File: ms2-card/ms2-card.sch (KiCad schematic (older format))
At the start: 41 parts, among them J1 Schaltregler, J10 MicroSD_SPI_CD, J11 I2C, J2 ESP Prog, J20 Smartcard Connector, J21 Card Edge, J22 Card Edge, J23 Conn_01x04, J3 RTS, J30 USB_B_Micro, J31 Power Select, J32 FTDI Adapter, J40 SP1, J50 Conn_01x05, J51 SP1, Q30 BC847, SW1 RESET, U1 ESP-12F, U30 CH330N, U40 ADUM1250, U41 ADuM1201AR

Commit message: wip
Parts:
- removed C1: 100uF, Capacitor_Tantalum_SMD:CP_EIA-7343-31_Kemet-D_Pad2.25x2.55mm_HandSolder, symbol Device:CP
- removed C30, C31, C40, C41, C50, C51: 100nF, Capacitors_SMD:C_0805_HandSoldering, symbol Device:C
- removed J1: Schaltregler, Connector_PinHeader_2.54mm:PinHeader_1x04_P2.54mm_Vertical, symbol Connector_Generic:Conn_01x04
- removed J2: ESP Prog, Connector_PinHeader_2.54mm:PinHeader_1x02_P2.54mm_Vertical, symbol Connector_Generic:Conn_01x02
- removed J3: RTS, Connector_PinHeader_2.54mm:PinHeader_1x01_P2.54mm_Vertical, symbol Connector_Generic:Conn_01x01
- removed J31: Power Select, Connector_PinHeader_2.54mm:PinHeader_1x03_P2.54mm_Vertical, symbol Connector_Generic:Conn_01x03
- removed J32: FTDI Adapter, Connector_PinSocket_2.54mm:PinSocket_1x06_P2.54mm_Horizontal, symbol Connector_Generic:Conn_01x06
- removed J40, J51: SP1, Connector_PinHeader_2.54mm:PinHeader_1x01_P2.54mm_Vertical, symbol Connector_Generic:Conn_01x01
- removed J50: Conn_01x05, Connector_PinHeader_2.54mm:PinHeader_1x05_P2.54mm_Vertical, symbol Connector_Generic:Conn_01x05
- removed R2, R50, R51: 4k7, Resistors_SMD:R_0805_HandSolderingII, symbol Device:R
- removed U1: ESP-12F, ESP8266:ESP-12E, symbol ESP8266:ESP-12F
- removed U30: CH330N, Package_SO:SOIC-8_3.9x4.9mm_P1.27mm, symbol Interface_USB:CH330N
- removed U40: ADUM1250, Package_SO:SOIC-8_3.9x4.9mm_P1.27mm, symbol Isolator:ADuM1201AR
- removed U41: ADuM1201AR, Package_SO:SOIC-8_3.9x4.9mm_P1.27mm, symbol Isolator:ADuM1201AR
- added Brd1: SSD1306, Lokkarten:128x64OLED, symbol Lokkarten:SSD1306
- added J1: Micro_SD_Card, w_conn_misc:GCT-MEM2055-00-190-01-A, symbol Connector:Micro_SD_Card
- added M1: PI_PICO_ZERO, Lokkarten:PI_PICO_ZERO, symbol Lokkarten:PI_PICO_ZERO
- added U1: W25Q128JVS, Package_SO:SOIC-8_5.23x5.23mm_P1.27mm, symbol Memory_Flash:W25Q128JVS
- J30: value USB_B_Micro -> Power Only
- SW1: value RESET -> SW_Push
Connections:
- net labels added: CS0, CS1
- net labels removed: CS, Card', GND2, GPIO0, LED, RxD, SCL', SDA', TxD, V3, VBUS, VDDA
- wire segments 180 -> 73
- no-connect marks 14 -> 5
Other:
- note removed: "Alternative zum CH330N"
- note removed: "Galvanische Trennung\nfür alt. RPi Interface"
- moved on the sheet: J21, J22, J30, Q30, R20, R21, R22, R23, R24

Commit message: new version with Pi Pico Zero
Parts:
- removed J1: Micro_SD_Card, w_conn_misc:GCT-MEM2055-00-190-01-A, symbol Connector:Micro_SD_Card
- removed J30: Power Only, Connector_USB:USB_Micro-B_Molex-105017-0001, symbol Connector:USB_B_Micro
- added C1: 100nF, Capacitor_SMD:C_0805_2012Metric_Pad1.18x1.45mm_HandSolder, symbol Device:C
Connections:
- net labels added: CLK0, CLK1, GP12, MISO0, MISO1, MOSI0, MOSI1, SCL0, SCL1, SDA0, SDA1
- net labels removed: CLK, MISO, MOSI, MS2PWR
- wire segments 73 -> 103
- no-connect marks 5 -> 14
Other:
- moved on the sheet: Brd1

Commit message: fix schematic
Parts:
- added C2: 100nF, Capacitor_SMD:C_0805_2012Metric_Pad1.18x1.45mm_HandSolder, symbol Device:C
- added J30: Power_Only, Connector_USB:USB_Micro-B_Molex-105017-0001, symbol Connector:USB_B_Micro
- added R2, R3: 4k7, Resistors_SMD:R_0805_HandSolderingII, symbol Device:R
- added R7, R8, R9: 47, Resistors_SMD:R_0805_HandSolderingII, symbol Device:R
- R6: renamed from R12; value 4k7 -> 47
- renumbered R11 to R4, R13 to R5
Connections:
- net SCL is gone; now on net SCL0: J20.3 (Pin_3)
- net SDA is gone; now on net SDA0: J20.6 (Pin_6)
- net +5V: now also J30.1 (VBUS)
- net CLK0: now also R8.1; no longer J10.5 (SCLK), R4.2
- net CS0: now also R4.2, R6.1; no longer J10.2 (~CS)
- net GND: now also C2.2, J30.5 (GND)
- net MISO0: now also R9.1; no longer J10.7 (DO)
- net MOSI0: now also R7.1; no longer J10.3 (DI), R6.2
- net VCC: now also C2.1, R2.1, R3.1; no longer R6.1
- net at U1.3 (IO2): now also R2.2
- net at U1.7 (IO3): now also R3.2
- new net: J10.2 (~CS), R6.2
- new net: J10.3 (DI), R7.2
- new net: J10.5 (SCLK), R8.2
- new net: J10.7 (DO), R9.2
- no-connect marks 14 -> 12
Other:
- moved on the sheet: R4, R5, R6

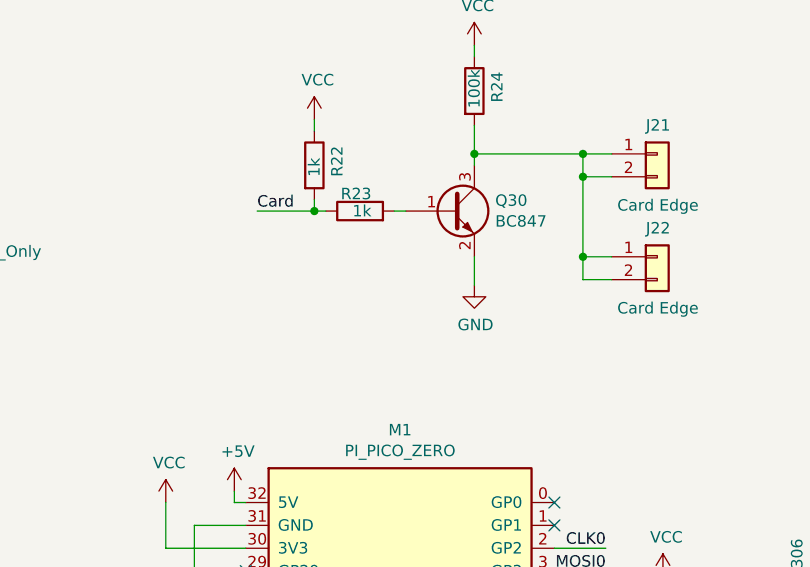
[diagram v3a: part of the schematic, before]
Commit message: add JP1 in schematic
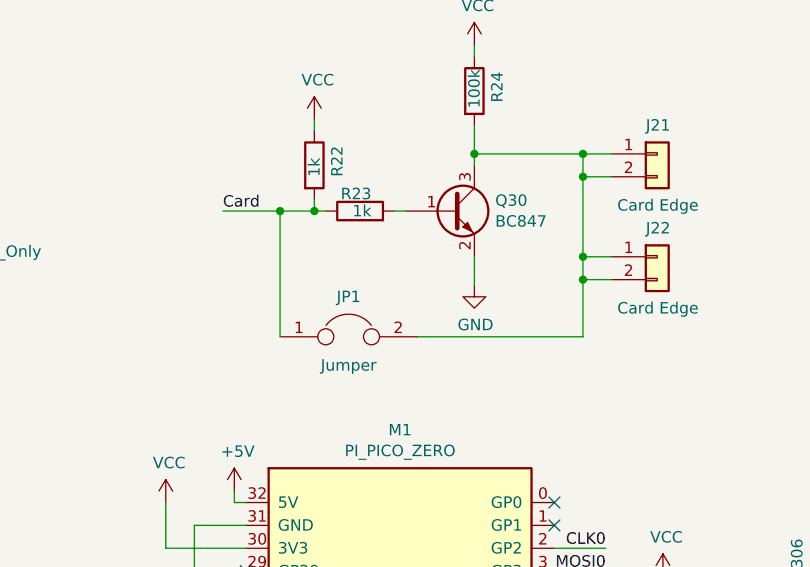
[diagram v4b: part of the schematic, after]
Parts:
- added JP1: Jumper, Jumper:SolderJumper-2_P1.3mm_Open_TrianglePad1.0x1.5mm, symbol Device:Jumper
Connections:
- net Card: now also JP1.1
- net at J21.1 (Pin_1), J21.2 (Pin_2), J22.1 (Pin_1)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: now also JP1.2
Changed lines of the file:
@@
 	1    0    0    -1
 $EndComp
-Text Label 6350 1975 0    50   ~ 0
+Text Label 6200 1975 0    50   ~ 0
 Card
 Connection ~ 6600 1975
 Wire Wire Line
-	6600 1975 6350 1975
+	6600 1975 6450 1975
 $Comp
 L power:GND #PWR0126
@@
 Wire Wire Line
 	5400 4300 5400 4625
+$Comp
+L Device:Jumper JP1
+U 1 1 623BDA57
+P 6750 2525
+F 0 "JP1" H 6750 2700 50  0000 C CNN
+F 1 "Jumper" H 6750 2400 50  0000 C CNN
+F 2 "Jumper:SolderJumper-2_P1.3mm_Open_TrianglePad1.0x1.5mm" H 6750 2525 50  0001 C CNN
+F 3 "~" H 6750 2525 50  0001 C CNN
+	1    6750 2525
+	1    0    0    -1
+$EndComp
+Wire Wire Line
+	6450 2525 6450 1975
+Connection ~ 6450 1975
+Wire Wire Line
+	6450 1975 6200 1975
+Wire Wire Line
+	7050 2525 7775 2525
+Wire Wire Line
+	7775 2525 7775 2275
+Connection ~ 7775 2275
 $EndSCHEMATC

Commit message: modified ground a little bit
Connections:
- net SCL0: now also M1.29 (GP29)
- net SDA0: now also M1.28 (GP28)
- no-connect marks 12 -> 10
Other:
- note added: "hand\nwire"
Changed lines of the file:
@@
 Sheet 1 1
 Title "Lokkarten Emulator"
-Date "2022-03-11"
+Date "2022-03-29"
 Rev "0.2"
 Comp "Modellbahn eXtreme"
@@
 Wire Wire Line
 	6300 3950 6050 3950
-Wire Wire Line
-	6300 4050 6050 4050
-Text Label 6050 3950 0    50   ~ 0
+Text Label 6050 3950 0    50   Italic 0
 SDA0
-Text Label 6050 4050 0    50   ~ 0
+Text Label 6050 4050 0    50   Italic 0
 SCL0
 Wire Wire Line
@@
 NoConn ~ 7650 3350
 Wire Wire Line
-	6300 3350 6075 3350
-Wire Wire Line
-	6300 3450 5950 3450
-Wire Wire Line
-	5950 3450 5950 3250
+	6300 3350 5775 3350
+Wire Wire Line
+	6300 3450 6000 3450
+Wire Wire Line
+	6000 3450 6000 3250
 $Comp
 L power:VCC #PWR0113
 U 1 1 623AA623
-P 5950 3250
-F 0 "#PWR0113" H 5950 3100 50  0001 C CNN
-F 1 "VCC" H 5965 3423 50  0000 C CNN
-F 2 "" H 5950 3250 50  0001 C CNN
-F 3 "" H 5950 3250 50  0001 C CNN
-	1    5950 3250
+P 6000 3250
+F 0 "#PWR0113" H 6000 3100 50  0001 C CNN
+F 1 "VCC" H 6015 3423 50  0000 C CNN
+F 2 "" H 6000 3250 50  0001 C CNN
+F 3 "" H 6000 3250 50  0001 C CNN
+	1    6000 3250
 	1    0    0    -1
 $EndComp
@@
 L power:GND #PWR0114
 U 1 1 623AAB7F
-P 6075 3575
-F 0 "#PWR0114" H 6075 3325 50  0001 C CNN
-F 1 "GND" H 6080 3402 50  0000 C CNN
-F 2 "" H 6075 3575 50  0001 C CNN
-F 3 "" H 6075 3575 50  0001 C CNN
-	1    6075 3575
-	1    0    0    -1
-$EndComp
-NoConn ~ 6300 3550
-NoConn ~ 6300 3650
+P 5775 3575
+F 0 "#PWR0114" H 5775 3325 50  0001 C CNN
+F 1 "GND" H 5780 3402 50  0000 C CNN
+F 2 "" H 5775 3575 50  0001 C CNN
+F 3 "" H 5775 3575 50  0001 C CNN
+	1    5775 3575
+	1    0    0    -1
+$EndComp
 NoConn ~ 6300 3750
 NoConn ~ 6300 3850
 Wire Wire Line
-	6075 3350 6075 3575
+	5775 3350 5775 3575
 NoConn ~ 2275 1650
 $Comp
@@
 	7775 2525 7775 2275
 Connection ~ 7775 2275
+Wire Wire Line
+	6050 3950 6050 3650
+Wire Wire Line
+	6050 3650 6300 3650
+Wire Wire Line
+	6000 4050 6000 3550
+Wire Wire Line
+	6000 3550 6300 3550
+Wire Wire Line
+	6000 4050 6300 4050
+Text Notes 5925 3850 0    50   ~ 0
+hand\nwire
 $EndSCHEMATC

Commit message: try to solve conflict
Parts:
- removed J11: I2C, Connector_PinHeader_2.54mm:PinHeader_1x05_P2.54mm_Vertical, symbol Connector_Generic:Conn_01x05
- removed JP1: Jumper, Jumper:SolderJumper-2_P1.3mm_Open_TrianglePad1.0x1.5mm, symbol Device:Jumper
- removed M1: PI_PICO_ZERO, Lokkarten:PI_PICO_ZERO, symbol Lokkarten:PI_PICO_ZERO
- removed Q30: BC847, Package_TO_SOT_SMD:SOT-23, symbol Transistor_BJT:BC847
- removed R22, R23: 1k, Resistors_SMD:R_0805_HandSolderingII, symbol Device:R
- removed R24: 100k, Resistors_SMD:R_0805_HandSolderingII, symbol Device:R
- added J11: Conn_01x06, Connector_PinHeader_2.54mm:PinHeader_1x06_P2.54mm_Vertical, symbol Connector_Generic:Conn_01x06
- added U1: RP2040, RP2040:RP2040-QFN-56, symbol MCU_RaspberryPi_RP2040:RP2040
- R6, R7: footprint Resistors_SMD:R_0805_HandSolderingII -> Resistor_SMD:R_0603_1608Metric_Pad0.98x0.95mm_HandSolder
- U2: renamed from U1; JLCPCB (none) -> C97521
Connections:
- net Card: now also J21.1 (Pin_1), J21.2 (Pin_2), J22.1 (Pin_1), J22.2 (Pin_2), J11.3 (Pin_3)
- net GND: now also J11.6 (Pin_6)
- net SCL0: now also J11.5 (Pin_5)
- net SDA0: now also J11.4 (Pin_4)
- net VCC: now also J11.1 (Pin_1)
- net MS2Power: now reaches J20.1 (Pin_1)
- net MS2Power: now also J11.2 (Pin_2)
- new net: U1.22 (IOVDD), U1.33 (IOVDD), U1.42 (IOVDD), U1.49 (IOVDD)
- no-connect marks 10 -> 5
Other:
- note removed: "hand\nwire"
- moved on the sheet: Brd1, C1, C2, D1, J10, J20, J21, J22, J23, J30, R1, R2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
